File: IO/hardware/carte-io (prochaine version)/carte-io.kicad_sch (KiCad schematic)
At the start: 0 parts

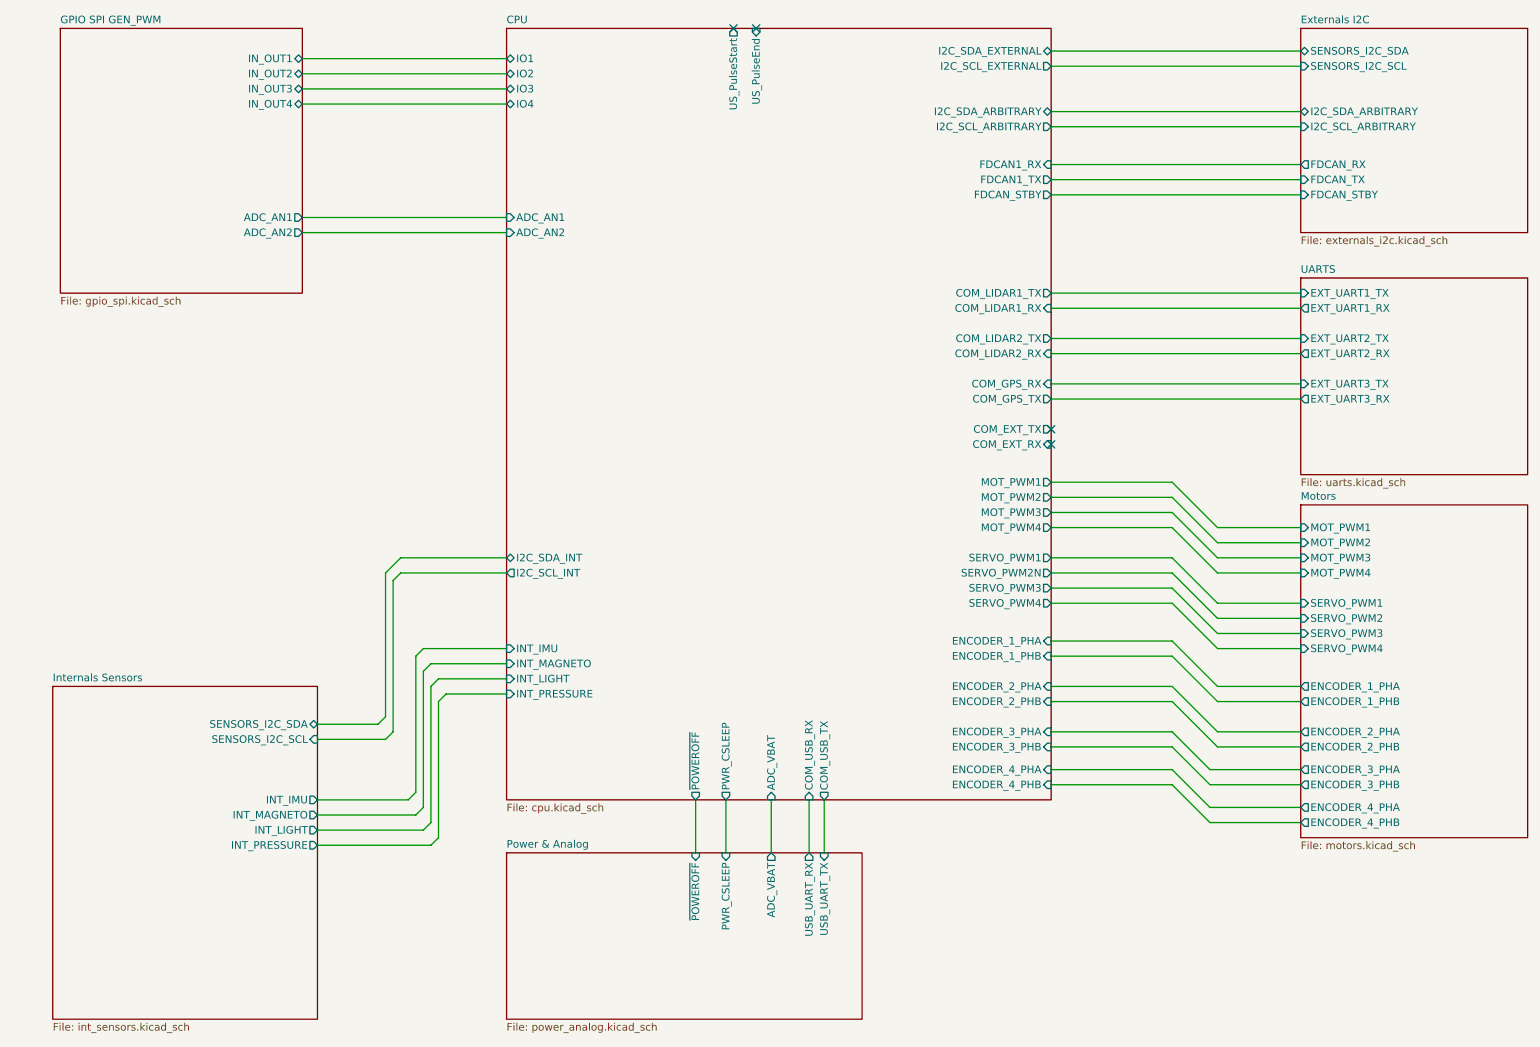
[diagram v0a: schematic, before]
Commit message: Recuperation de la carte IO perdue lors de la suppression des 3 derniers commit
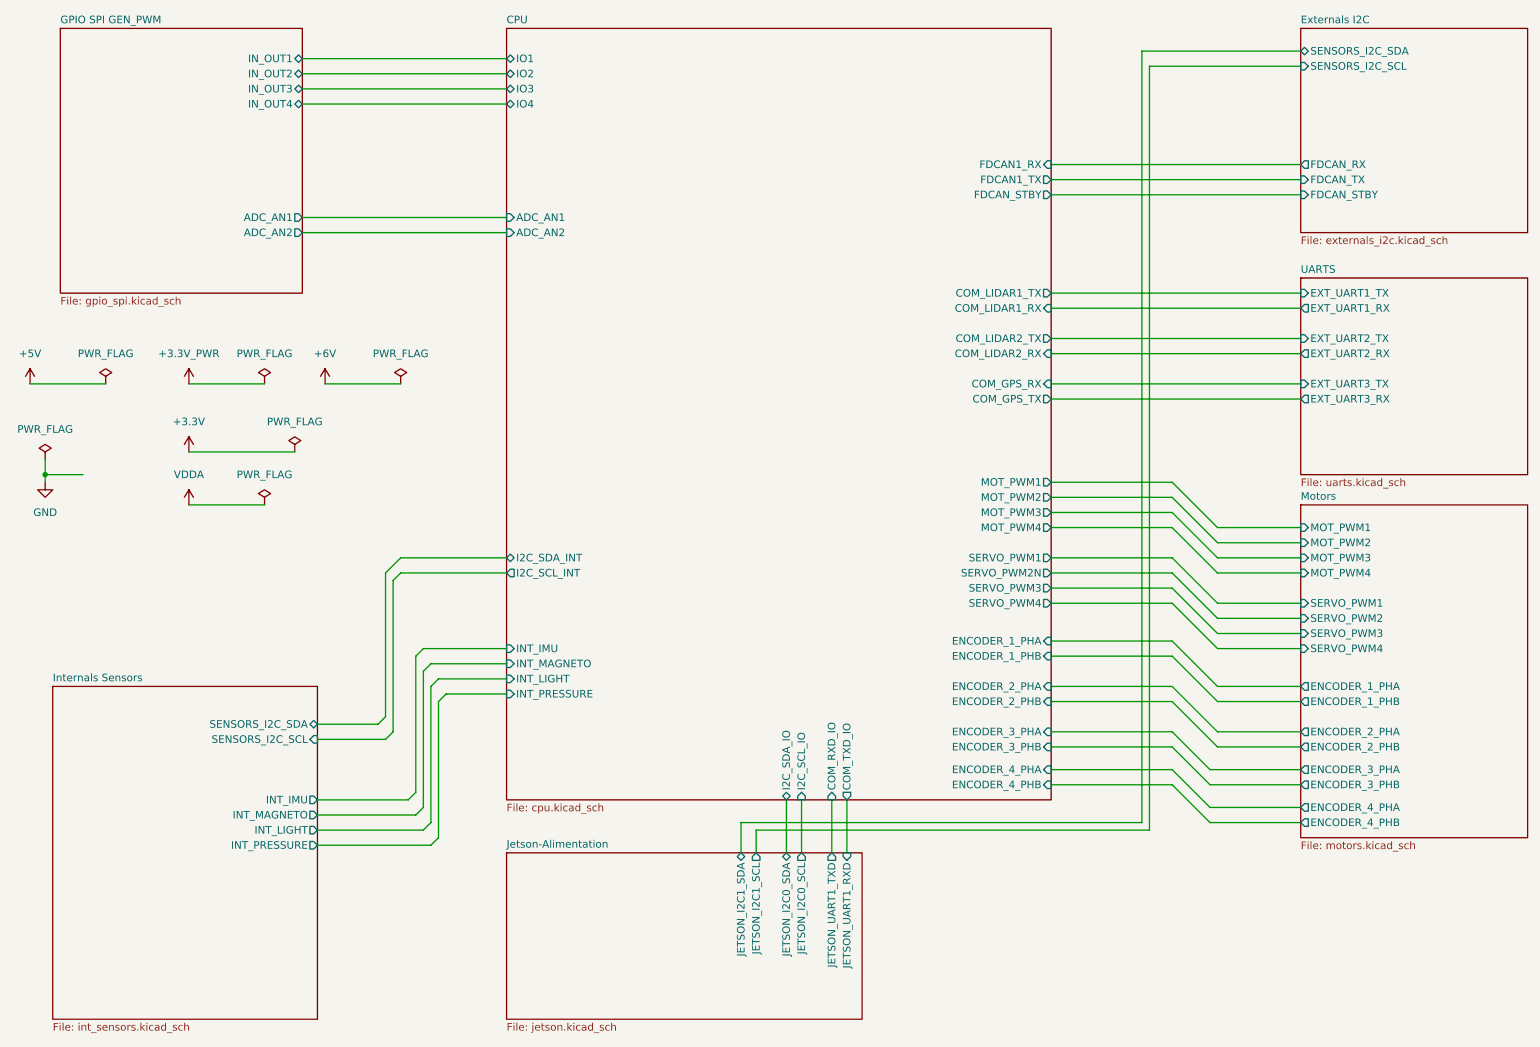
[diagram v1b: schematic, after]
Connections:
- no-connect marks 4 -> 0
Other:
- sheet Power & Analog renamed Jetson-Alimentation
- sheet CPU ports: added COM_RXD_IO, COM_TXD_IO, I2C_SCL_IO, I2C_SDA_IO; removed ADC_VBAT, COM_EXT_RX, COM_EXT_TX, COM_USB_RX, COM_USB_TX, I2C_SCL_ARBITRARY, I2C_SCL_EXTERNAL, I2C_SDA_ARBITRARY, I2C_SDA_EXTERNAL, PWR_CSLEEP, US_PulseEnd, US_PulseStart, ~{POWEROFF}
- sheet Externals I2C ports: added none; removed I2C_SCL_ARBITRARY, I2C_SDA_ARBITRARY
- sheet Jetson-Alimentation: file power_analog.kicad_sch -> jetson.kicad_sch
- sheet Jetson-Alimentation ports: added JETSON_I2C0_SCL, JETSON_I2C0_SDA, JETSON_I2C1_SCL, JETSON_I2C1_SDA, JETSON_UART1_RXD, JETSON_UART1_TXD; removed ADC_VBAT, PWR_CSLEEP, USB_UART_RX, USB_UART_TX, ~{POWEROFF}
